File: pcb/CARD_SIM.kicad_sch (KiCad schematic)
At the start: 1 part, among them J6 MSIM-11-C

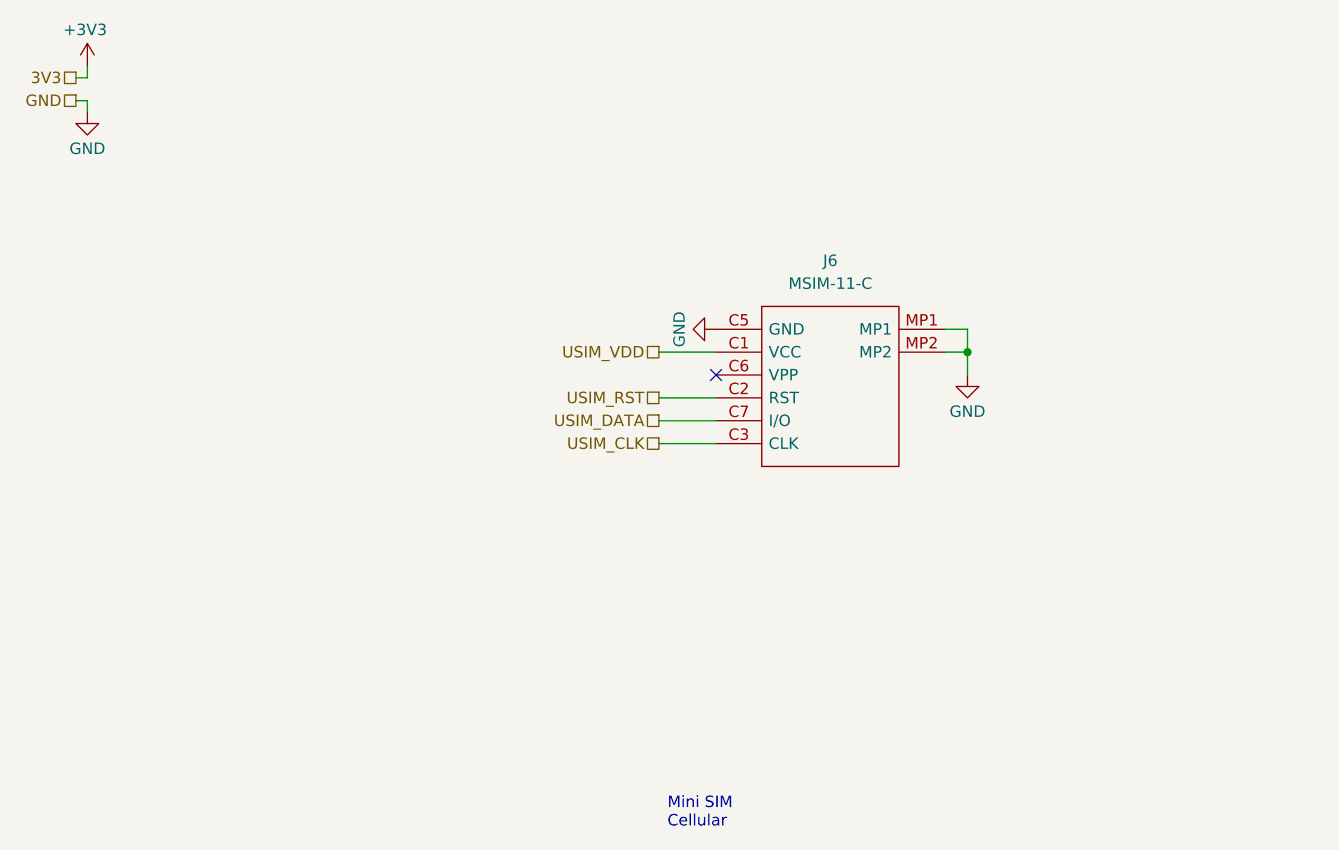
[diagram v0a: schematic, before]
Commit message: updated pcie sd and sim cards
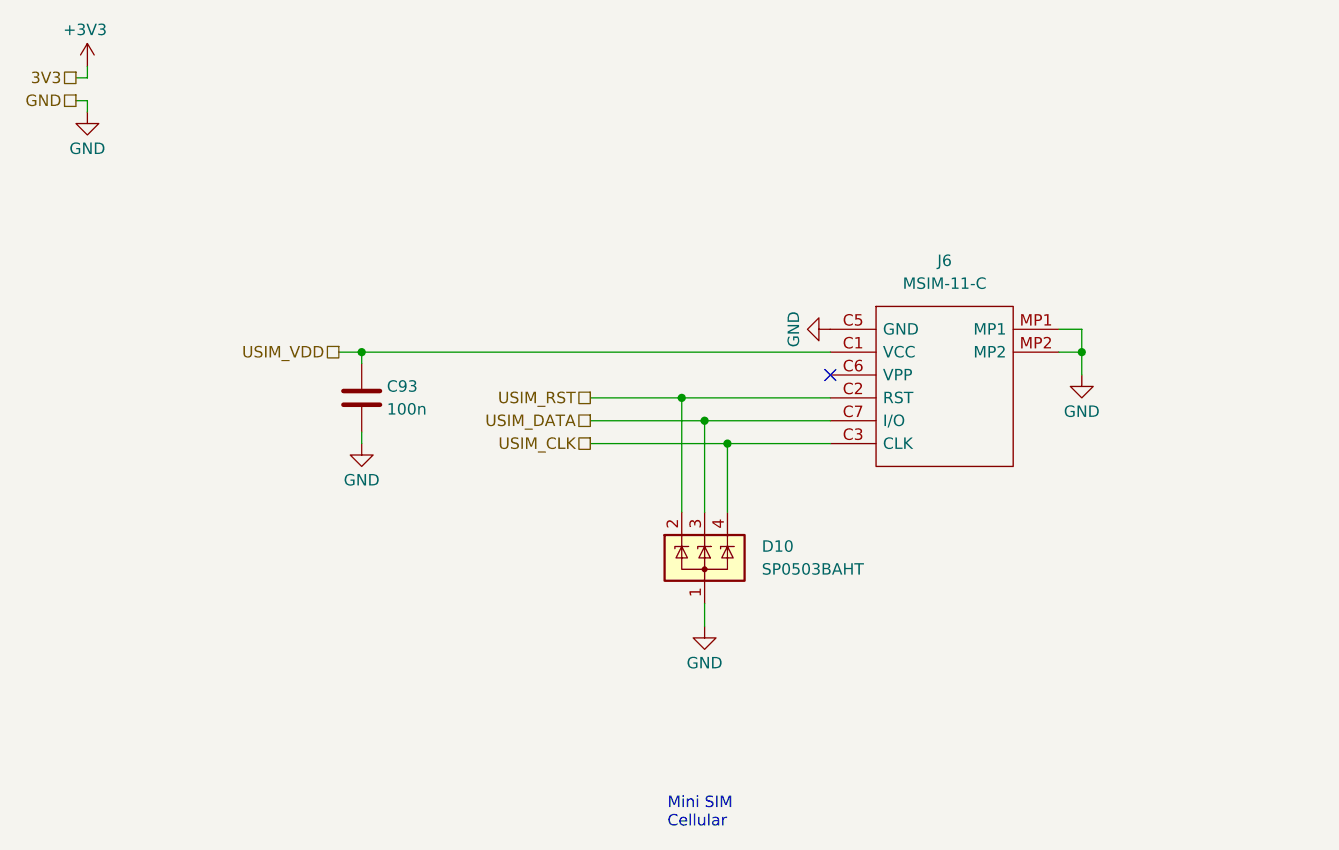
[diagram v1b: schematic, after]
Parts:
- added C93: 100n, Capacitor_SMD:C_0603_1608Metric_Pad1.08x0.95mm_HandSolder, symbol Device:C
- added D10: SP0503BAHT, Package_TO_SOT_SMD:SOT-143, symbol Power_Protection:SP0503BAHT
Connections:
- net GND: now also C93.2, D10.1 (A)
- net USIM_CLK: now also D10.4 (K)
- net USIM_DATA: now also D10.3 (K)
- net USIM_RST: now also D10.2 (K)
- net USIM_VDD: now also C93.1
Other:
- moved on the sheet: J6

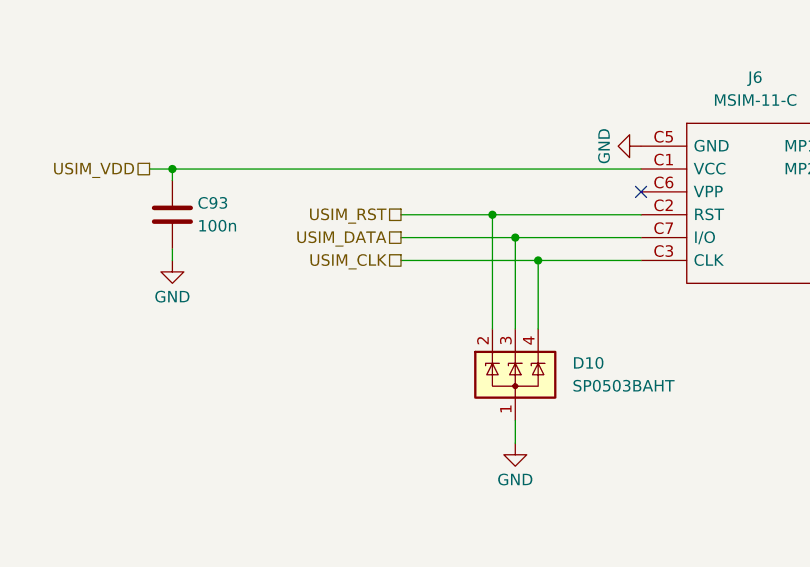
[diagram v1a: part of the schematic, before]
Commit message: reannotated, updated some symbols
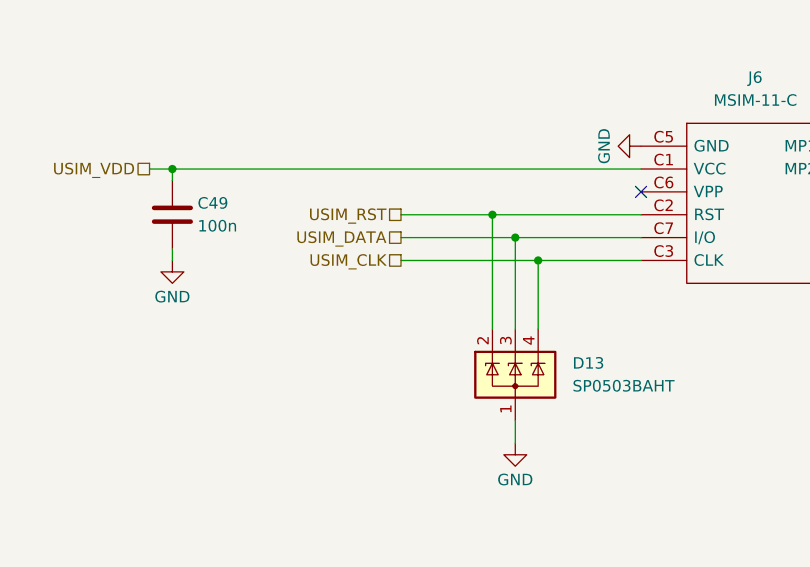
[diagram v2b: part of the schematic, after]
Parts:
- renumbered C93 to C49, D10 to D13
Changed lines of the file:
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@@
 		(on_board yes)
 		(dnp no)
-		(property "Reference" "#PWR0414"
+		(property "Reference" "#PWR0251"
 			(at 57.15 72.39 0)
 			(effects
@@
 			(project "NCU"
 				(path "/3aee14c3-5480-4f7c-989e-3fef81779034/9e564c38-7205-44f8-b5f6-41c7c4a47ab0"
-					(reference "#PWR0414")
+					(reference "#PWR0251")
 					(unit 1)
 				)
@@
 		(on_board yes)
 		(dnp no)
-		(property "Reference" "C93"
+		(property "Reference" "C49"
 			(at 59.944 59.69 0)
 			(effects
@@
 			(project "NCU"
 				(path "/3aee14c3-5480-4f7c-989e-3fef81779034/9e564c38-7205-44f8-b5f6-41c7c4a47ab0"
-					(reference "C93")
+					(reference "C49")
 					(unit 1)
 				)
@@
 		(on_board yes)
 		(dnp no)
-		(property "Reference" "#PWR0415"
+		(property "Reference" "#PWR0253"
 			(at 95.25 92.71 0)
 			(effects
@@
 			(project "NCU"
 				(path "/3aee14c3-5480-4f7c-989e-3fef81779034/9e564c38-7205-44f8-b5f6-41c7c4a47ab0"
-					(reference "#PWR0415")
+					(reference "#PWR0253")
 					(unit 1)
 				)
@@
 		(on_board yes)
 		(dnp no)
-		(property "Reference" "#PWR0197"
+		(property "Reference" "#PWR0254"
 			(at 102.87 53.34 0)
 			(effects
@@
 			(project "NCU"
 				(path "/3aee14c3-5480-4f7c-989e-3fef81779034/9e564c38-7205-44f8-b5f6-41c7c4a47ab0"
-					(reference "#PWR0197")
+					(reference "#PWR0254")
 					(unit 1)
 				)
@@
 		(on_board yes)
 		(dnp no)
-		(property "Reference" "#PWR0199"
+		(property "Reference" "#PWR0258"
 			(at 137.16 64.77 0)
 			(effects
@@
 			(project "NCU"
 				(path "/3aee14c3-5480-4f7c-989e-3fef81779034/9e564c38-7205-44f8-b5f6-41c7c4a47ab0"
-					(reference "#PWR0199")
+					(reference "#PWR0258")
 					(unit 1)
 				)
@@
 		(on_board yes)
 		(dnp no)
-		(property "Reference" "#PWR0193"
+		(property "Reference" "#PWR0247"
 			(at 26.67 27.94 0)
 			(effects
@@
 			(project "NCU"
 				(path "/3aee14c3-5480-4f7c-989e-3fef81779034/9e564c38-7205-44f8-b5f6-41c7c4a47ab0"
-					(reference "#PWR0193")
+					(reference "#PWR0247")
 					(unit 1)
 				)
@@
 		(dnp no)
 		(fields_autoplaced yes)
-		(property "Reference" "D10"
+		(property "Reference" "D13"
 			(at 101.6 77.4699 0)
 			(effects
@@
 			(project "NCU"
 				(path "/3aee14c3-5480-4f7c-989e-3fef81779034/9e564c38-7205-44f8-b5f6-41c7c4a47ab0"
-					(reference "D10")
+					(reference "D13")
 					(unit 1)
 				)
@@
 		(on_board yes)
 		(dnp no)
-		(property "Reference" "#PWR0194"
+		(property "Reference" "#PWR0248"
 			(at 26.67 35.56 0)
 			(effects
@@
 			(project "NCU"
 				(path "/3aee14c3-5480-4f7c-989e-3fef81779034/9e564c38-7205-44f8-b5f6-41c7c4a47ab0"
-					(reference "#PWR0194")
-					(unit 1)
-				)
+					(reference "#PWR0248")
+					(unit 1)
+				)

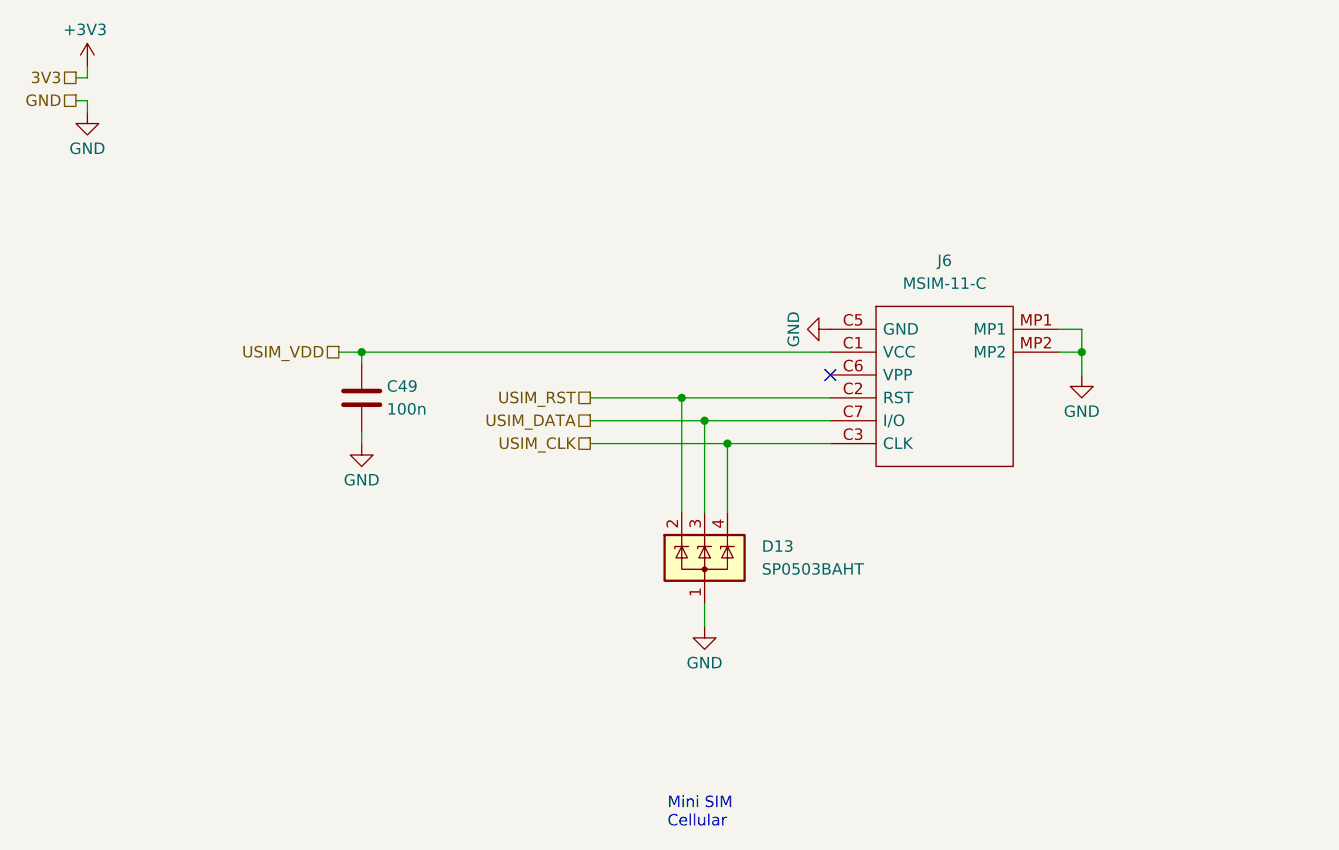
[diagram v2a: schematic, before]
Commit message: swapped sd to micro sd
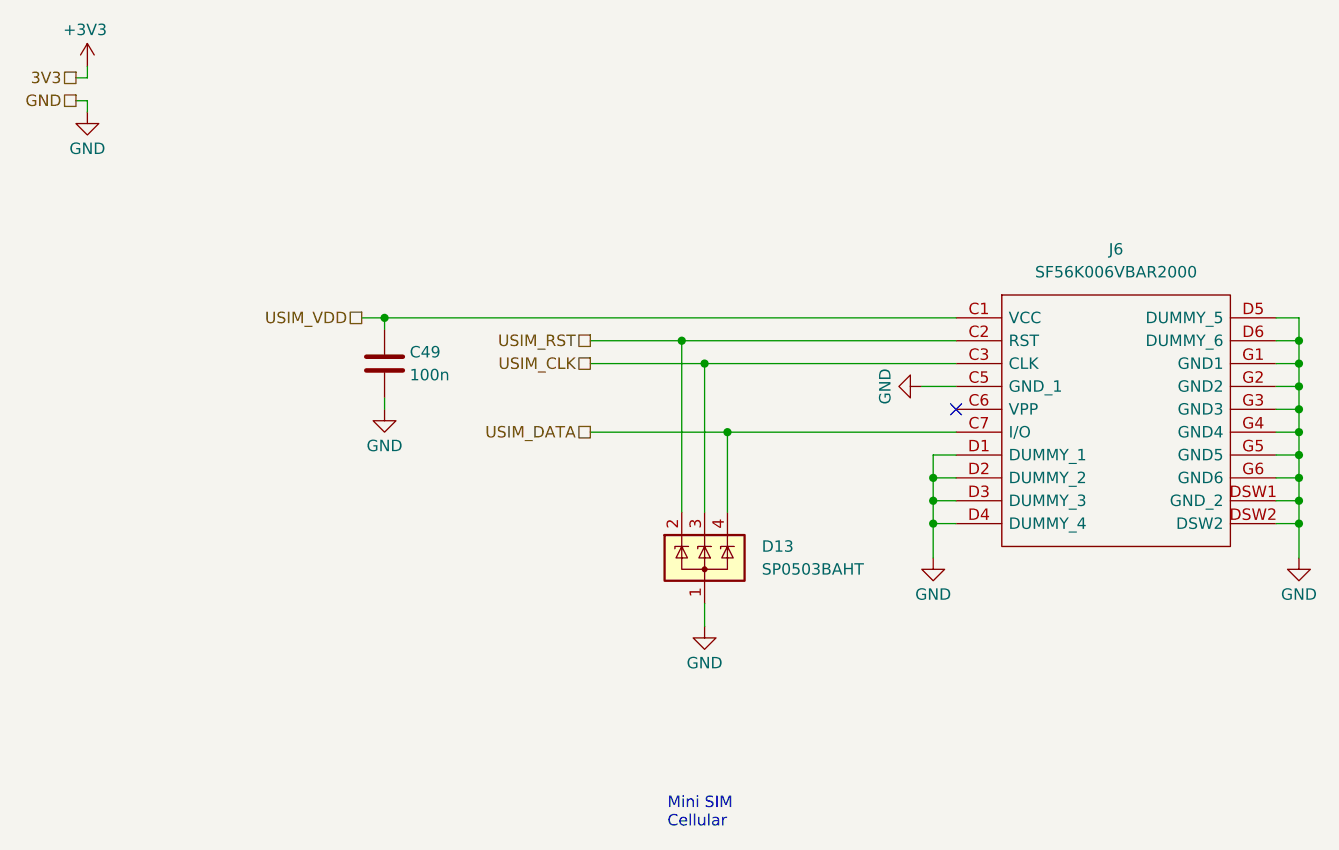
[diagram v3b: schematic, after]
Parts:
- removed J6: MSIM-11-C, MSIM11C, symbol 0_SamacSys_Parts:MSIM-11-C
- added J6: SF56K006VBAR2000, SF56K006VBAR2000, symbol 0_SamacSys_Parts:SF56K006VBAR2000
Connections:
- net GND: now also J6.C5 (GND_1), J6.D1 (DUMMY_1), J6.D2 (DUMMY_2), J6.D3 (DUMMY_3), J6.D4 (DUMMY_4), J6.D5 (DUMMY_5), J6.D6 (DUMMY_6), J6.DSW1 (GND_2), J6.DSW2, J6.G1 (GND1), J6.G2 (GND2), J6.G3 (GND3), J6.G4 (GND4), J6.G5 (GND5), J6.G6 (GND6)
- net USIM_CLK: now also D13.3 (K), J6.C3 (CLK); no longer D13.4 (K)
- net USIM_DATA: now also D13.4 (K), J6.C7 (I/O); no longer D13.3 (K)
- net USIM_RST: now also J6.C2 (RST)
- net USIM_VDD: now also J6.C1 (VCC)
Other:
- moved on the sheet: C49
